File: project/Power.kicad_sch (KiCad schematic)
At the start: 20 parts

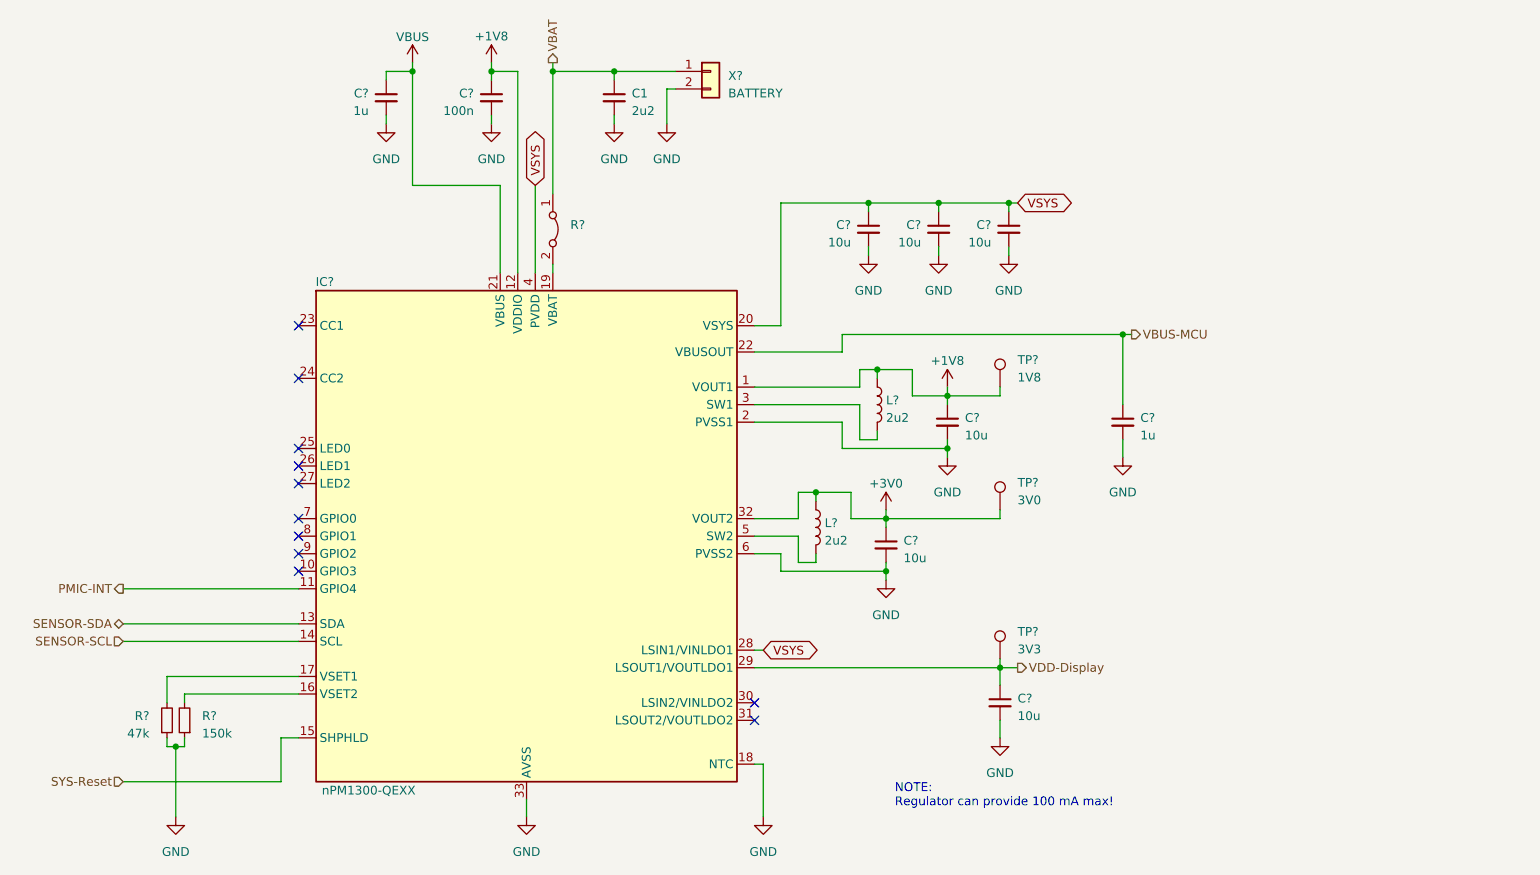
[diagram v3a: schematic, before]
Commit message: - Remove old documentation - Update libraries - Rename signals - Update CHANGELOG
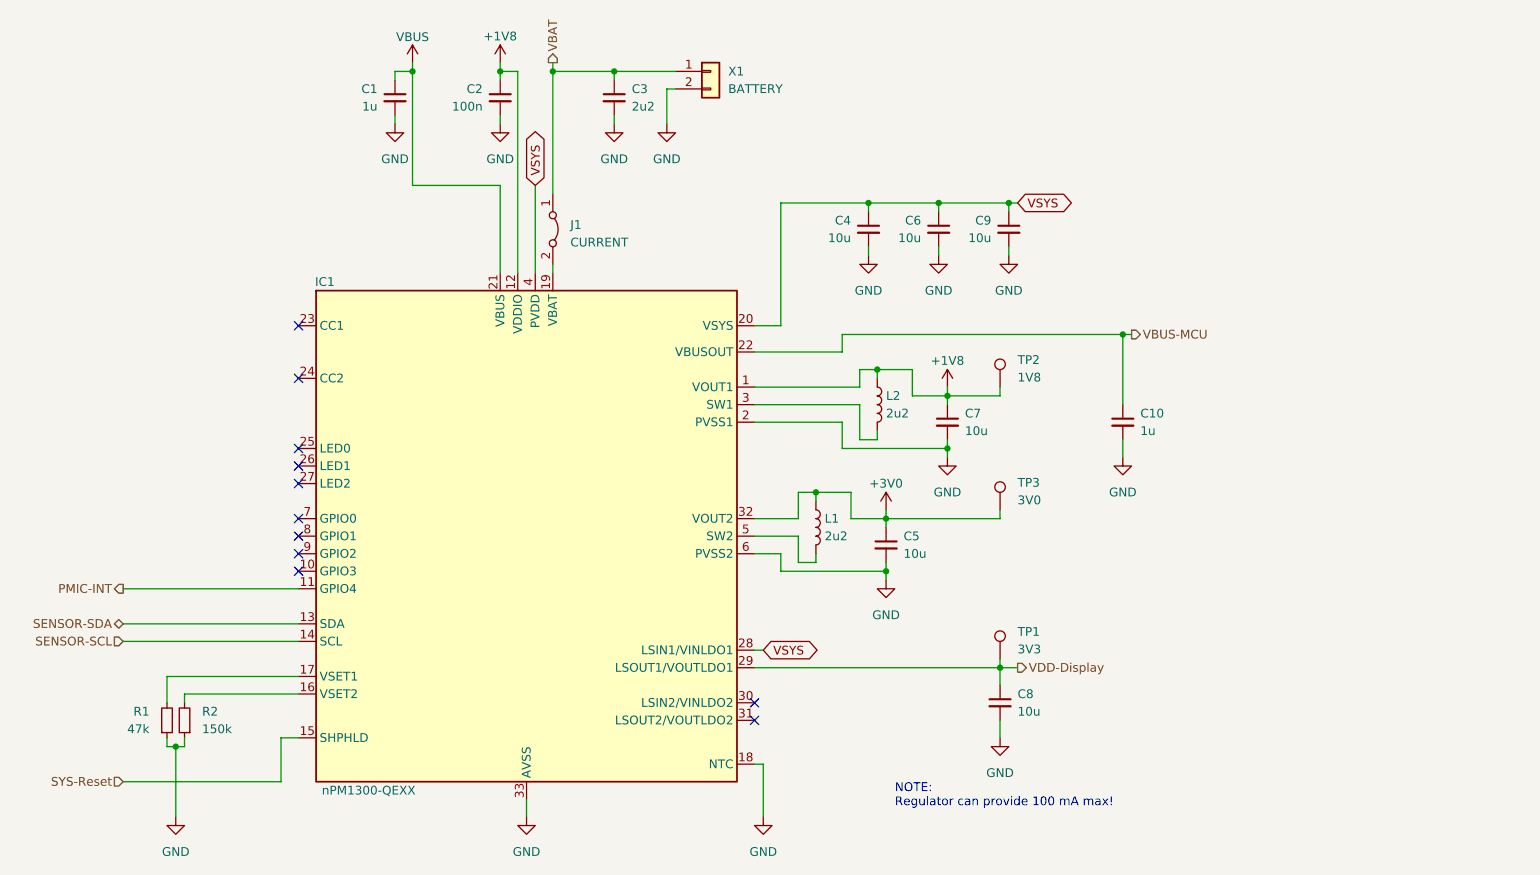
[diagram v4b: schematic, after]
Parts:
- J1: renamed from R?; value ~ -> CURRENT
- gave numbers to parts that had none: 18
- renumbered C1 to C3
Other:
- moved on the sheet: C1, C2

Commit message: Update README, replace current measurement jumper with 0402 resistor on TOP side, update footprints and symbols
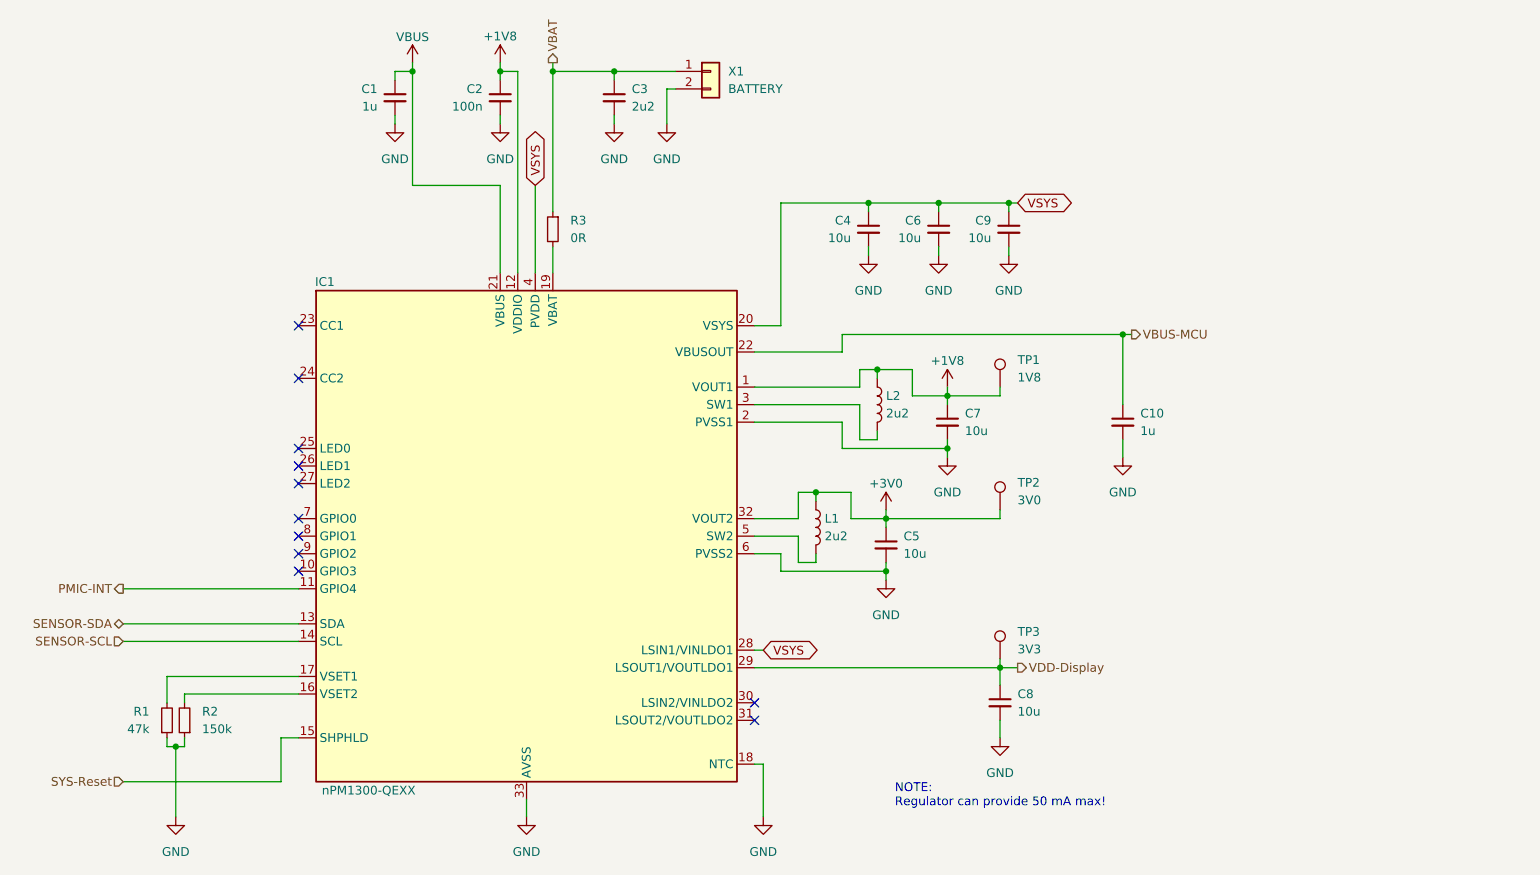
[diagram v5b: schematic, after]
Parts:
- removed J1: CURRENT, Jumper:SolderJumper-2_P1.3mm_Bridged_Pad1.0x1.5mm, symbol Jumper:Jumper_2_Bridged
- added R3: 0R, Resistor_SMD:R_0402_1005Metric, symbol Device:R_Small
- renumbered TP2 to TP1, TP3 to TP2, TP1 to TP3
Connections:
- net VBAT: now also R3.1
- net at IC1.19 (VBAT): now also R3.2
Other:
- note added: "NOTE: Regulator can provide 50 mA max!"
- note removed: "NOTE: Regulator can provide 100 mA max!"
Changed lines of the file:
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@@
     (stroke (width 0) (type default))
   )
-  (wire (pts (xy 135.89 40.64) (xy 135.89 58.42))
+  (wire (pts (xy 135.89 40.64) (xy 135.89 60.96))
     (stroke (width 0) (type default))
   )
@@
     (stroke (width 0) (type default))
   )
-  (wire (pts (xy 135.89 68.58) (xy 135.89 69.85))
+  (wire (pts (xy 135.89 66.04) (xy 135.89 69.85))
     (stroke (width 0) (type default))
   )
@@
     (stroke (width 0) (type default))
   )
-  (text "NOTE:\nRegulator can provide 100 mA max!" (at 185.42 147.32 0)
+  (text "NOTE:\nRegulator can provide 50 mA max!" (at 185.42 147.32 0)
     (effects (font (size 1.27 1.27)) (justify left bottom))
   )
@@
   (symbol (lib_id "Connector:TestPoint") (at 200.66 125.73 0) (unit 1)
     (in_bom no) (on_board yes) (dnp no) (fields_autoplaced)
-    (property "Reference" "TP1" (at 203.2 121.793 0)
+    (property "Reference" "TP3" (at 203.2 121.793 0)
       (effects (font (size 1.27 1.27)) (justify left))
     )
@@
       (project "ZSWatch"
         (path "/d5742f03-3b1a-42e5-a384-018bd4b919aa/cee9a3a2-28cd-4e6c-b23d-337f115f39e8"
-          (reference "TP1") (unit 1)
+          (reference "TP3") (unit 1)
         )
       )
@@
     )
   )
+  (symbol (lib_id "Device:R_Small") (at 135.89 63.5 0) (mirror y) (unit 1)
+    (in_bom no) (on_board yes) (dnp no) (fields_autoplaced)
+    (property "Reference" "R3" (at 138.43 62.23 0)
+      (effects (font (size 1.27 1.27)) (justify right))
+    )
+    (property "Value" "0R" (at 138.43 64.77 0)
+      (effects (font (size 1.27 1.27)) (justify right))
+    )
+    (property "Footprint" "Resistor_SMD:R_0402_1005Metric" (at 135.89 63.5 0)
+      (effects (font (size 1.27 1.27)) hide)
+    )
+    (property "Datasheet" "~" (at 135.89 63.5 0)
+      (effects (font (size 1.27 1.27)) hide)
+    )
+    (property "Distributor" "Mouser" (at 135.89 63.5 0)
+      (effects (font (size 1.27 1.27)) hide)
+    )
+    (property "Mfr." "Bourns" (at 135.89 63.5 0)
+      (effects (font (size 1.27 1.27)) hide)
+    )
+    (property "Mfr. No." "CR0603-J/-000ELF" (at 135.89 63.5 0)
+      (effects (font (size 1.27 1.27)) hide)
+    )
+    (property "Order Number" "652-CR0603-J/-000ELF" (at 135.89 63.5 0)
+      (effects (font (size 1.27 1.27)) hide)
+    )
+    (property "CONFIG" "" (at 135.89 63.5 0)
+      (effects (font (size 1.27 1.27)) hide)
+    )
+    (pin "1")
+    (pin "2")
+    (instances
+      (project "ZSWatch"
+        (path "/d5742f03-3b1a-42e5-a384-018bd4b919aa/cee9a3a2-28cd-4e6c-b23d-337f115f39e8"
+          (reference "R3") (unit 1)
+        )
+      )
+    )
+  )
   (symbol (lib_id "power:GND") (at 113.03 48.26 0) (unit 1)
     (in_bom yes) (on_board yes) (dnp no) (fields_autoplaced)
@@
         (path "/d5742f03-3b1a-42e5-a384-018bd4b919aa/cee9a3a2-28cd-4e6c-b23d-337f115f39e8"
           (reference "#PWR02") (unit 1)
-        )
-      )
-    )
-  )
-  (symbol (lib_id "Jumper:Jumper_2_Bridged") (at 135.89 63.5 270) (unit 1)
-    (in_bom no) (on_board yes) (dnp no) (fields_autoplaced)
-    (property "Reference" "J1" (at 138.43 62.865 90)
-      (effects (font (size 1.27 1.27)) (justify left))
-    )
-    (property "Value" "CURRENT" (at 138.43 65.405 90)
-      (effects (font (size 1.27 1.27)) (justify left))
-    )
-    (property "Footprint" "Jumper:SolderJumper-2_P1.3mm_Bridged_Pad1.0x1.5mm" (at 135.89 63.5 0)
-      (effects (font (size 1.27 1.27)) hide)
-    )
-    (property "Datasheet" "~" (at 135.89 63.5 0)
-      (effects (font (size 1.27 1.27)) hide)
-    )
-    (property "Distributor" "" (at 135.89 63.5 0)
-      (effects (font (size 1.27 1.27)) hide)
-    )
-    (property "Mfr." "" (at 135.89 63.5 0)
-      (effects (font (size 1.27 1.27)) hide)
-    )
-    (property "Mfr. No." "" (at 135.89 63.5 0)
-      (effects (font (size 1.27 1.27)) hide)
-    )
-    (property "Order Number" "" (at 135.89 63.5 0)
-      (effects (font (size 1.27 1.27)) hide)
-    )
-    (property "CONFIG" "" (at 135.89 63.5 0)
-      (effects (font (size 1.27 1.27)) hide)
-    )
-    (pin "1")
-    (pin "2")
-    (instances
-      (project "ZSWatch"
-        (path "/d5742f03-3b1a-42e5-a384-018bd4b919aa/cee9a3a2-28cd-4e6c-b23d-337f115f39e8"
-          (reference "J1") (unit 1)
         )
       )
@@
   (symbol (lib_id "Connector:TestPoint") (at 200.66 104.14 0) (unit 1)
     (in_bom no) (on_board yes) (dnp no) (fields_autoplaced)
-    (property "Reference" "TP3" (at 203.2 100.203 0)
+    (property "Reference" "TP2" (at 203.2 100.203 0)
       (effects (font (size 1.27 1.27)) (justify left))
     )
@@
       (project "ZSWatch"
         (path "/d5742f03-3b1a-42e5-a384-018bd4b919aa/cee9a3a2-28cd-4e6c-b23d-337f115f39e8"
-          (reference "TP3") (unit 1)
+          (reference "TP2") (unit 1)
         )
       )
@@
   (symbol (lib_id "Connector:TestPoint") (at 200.66 86.36 0) (unit 1)
     (in_bom no) (on_board yes) (dnp no) (fields_autoplaced)
-    (property "Reference" "TP2" (at 203.2 82.423 0)
+    (property "Reference" "TP1" (at 203.2 82.423 0)
       (effects (font (size 1.27 1.27)) (justify left))
     )
@@
       (project "ZSWatch"
         (path "/d5742f03-3b1a-42e5-a384-018bd4b919aa/cee9a3a2-28cd-4e6c-b23d-337f115f39e8"
-          (reference "TP2") (unit 1)
-        )
-      )
+          (reference "TP1") (unit 1)
+        )
+      )

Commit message: Replace I2C mic with SPK0641HT4H-1
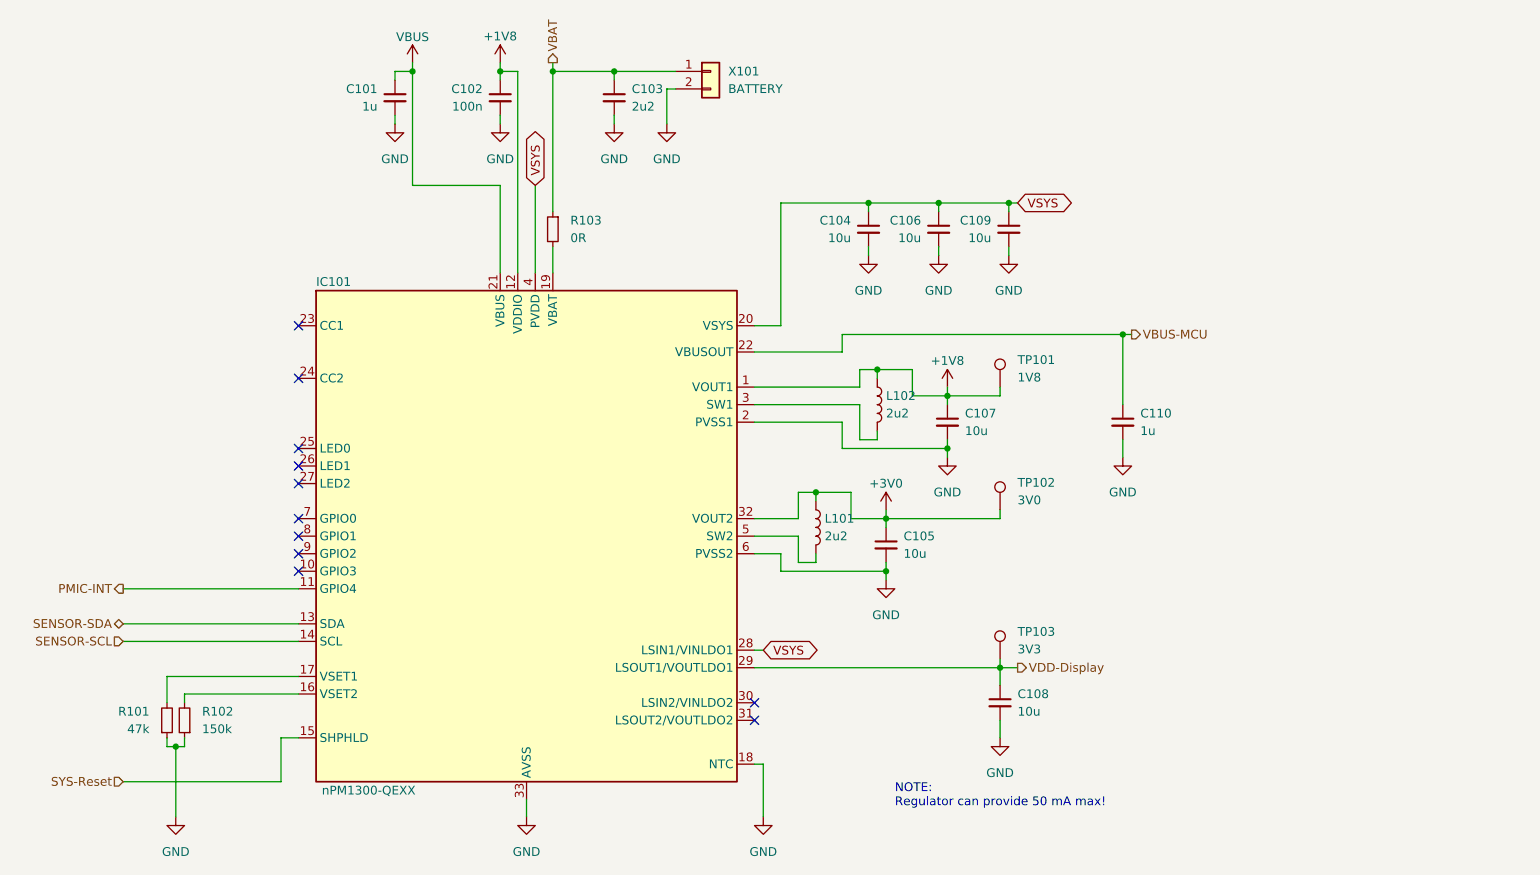
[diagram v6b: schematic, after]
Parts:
- renumbered C1 to C101, C2 to C102, C3 to C103, C4 to C104, C5 to C105, C6 to C106, C7 to C107, C8 to C108, C9 to C109, C10 to C110, IC1 to IC101, L1 to L101, L2 to L102, R1 to R101, R2 to R102, R3 to R103, TP1 to TP101, TP2 to TP102, TP3 to TP103, X1 to X101
